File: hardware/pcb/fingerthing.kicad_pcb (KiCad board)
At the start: 4 copper layers, 34 x 48 mm, 46 parts, among them J1 DX07S016JA1R1500, J2 R503, J4 SM03B-SRSS-TB(LF)(SN), SW1 434133025816, SW3 434133025816, U1 RP2350A, U2 NCP1117ST33T3G, U3 W25Q128JVSIQ, U4 USBLC6-2SC6, X1 12MHz

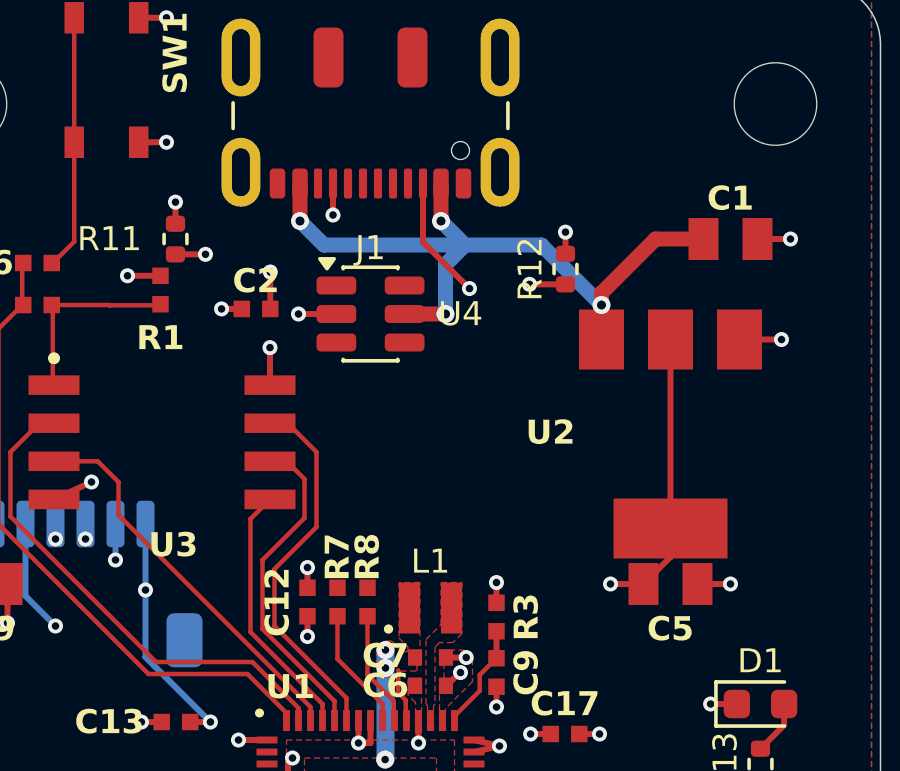
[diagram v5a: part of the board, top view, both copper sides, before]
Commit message: usb data / stackup
All PCB nets are routed. ERC, DRC and schematic parity pass with zero unconnected items and no exclusions. USB geometry follows the JLCPCB calculator result for JLC04161H-7628: 0.235 mm width, 0.15 mm pair gap and 0.25 mm ground clearance. Connector joins and ESD fan-out remain partly uncoupled and need final review.
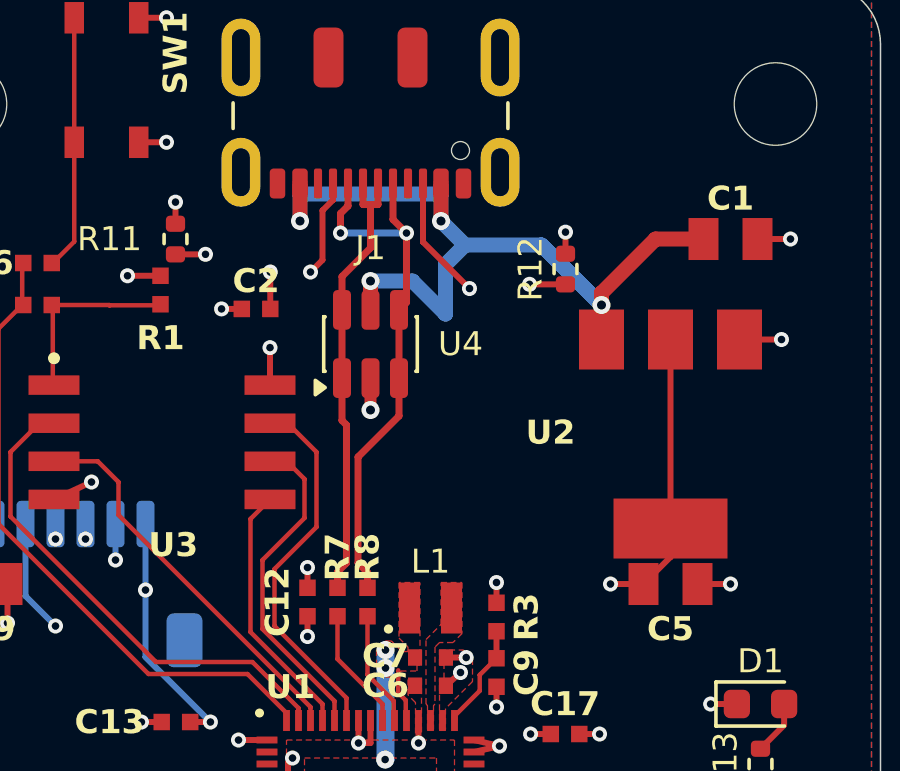
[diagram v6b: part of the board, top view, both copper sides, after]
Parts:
- moved U4 1.00 mm to (17.0, 12.0), turned to 90 degrees
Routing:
- net /USB_D-: track 0.00 -> 18.4 mm, vias 0 -> 2
- net /USB_D+: track 0.00 -> 15.3 mm
- net /VBUS: track 24.5 -> 30.5 mm
- net /CC2: track 11.3 -> 14.0 mm

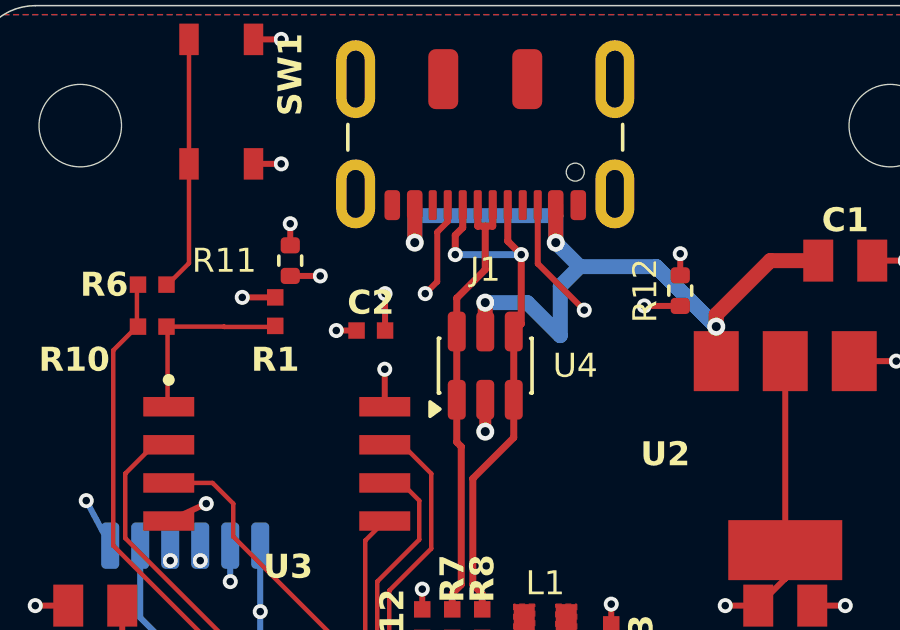
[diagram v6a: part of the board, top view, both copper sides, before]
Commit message: esd bypass / sensor pinout
Added the USBLC6-2 VBUS bypass from the ST layout example. ERC, DRC and schematic parity pass with zero unconnected items. The R503 pinout follows GROW manual 2019.6 v1.1. Its MX1.0 plug needs a verified adapter cable for the board JST SH socket.
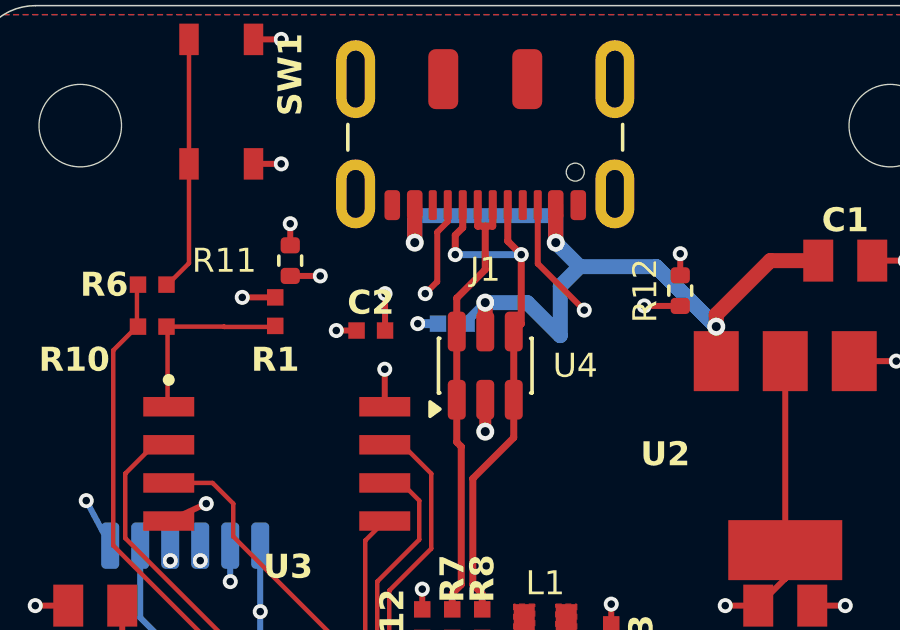
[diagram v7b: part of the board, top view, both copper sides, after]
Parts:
- added C20: 100n, RPI_COMPILED:generic_capc1005x50, B.Cu at (15.9, 10.6)
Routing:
- net /VBUS: track 30.5 -> 31.5 mm
- net /GND: track 32.3 -> 33.0 mm, vias 35 -> 36
